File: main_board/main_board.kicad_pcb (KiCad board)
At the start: 4 copper layers, 50 x 50 mm, 80 parts, among them J1 USB Port, J2 I2C, J3 LED, J4 Left_Mic, J5 Left_Speaker, J6 Right_Mic, J7 Right_Speaker, J8 I2C, Q1 MMBT3904, Q2 MMBT3904, SW1 SW_Push, SW2 SW_Push, SW3 SW_Push, U1 AMS1117-3.3, U2 CH340K, U4 Headphone Jack, U5 WM8988LGECN/V, U6 WM8988LGECN/V, U7 AMS1117-3.3, U8 ESP32-WROOM-32E

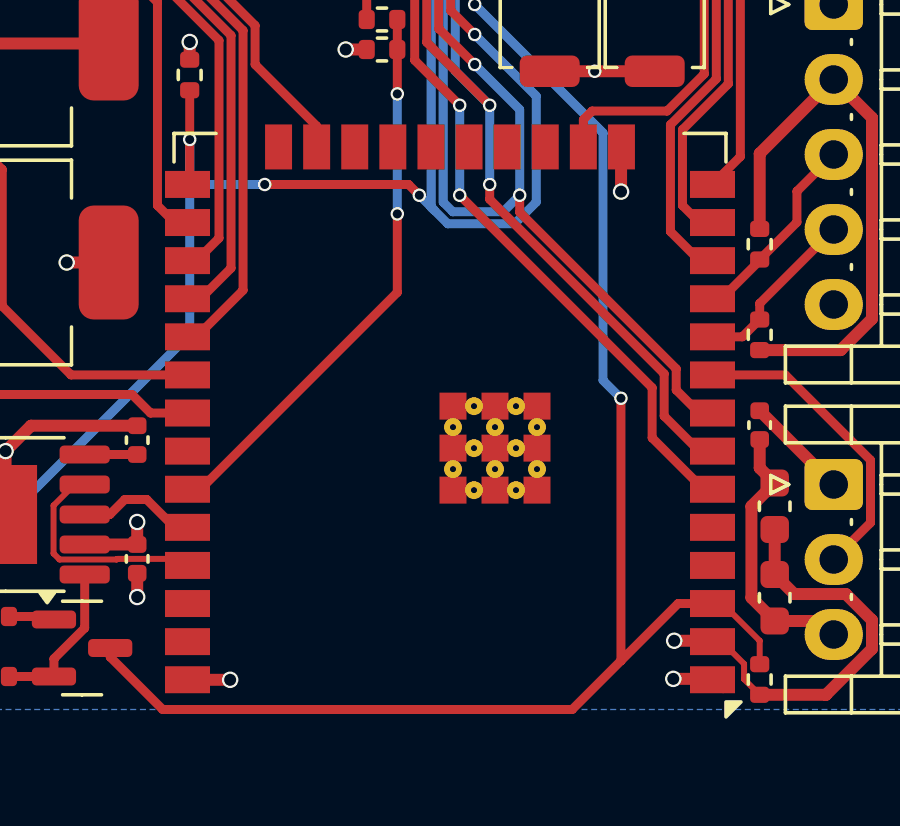
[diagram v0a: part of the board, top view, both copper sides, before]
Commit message: reroute SPI (non output pin issue)
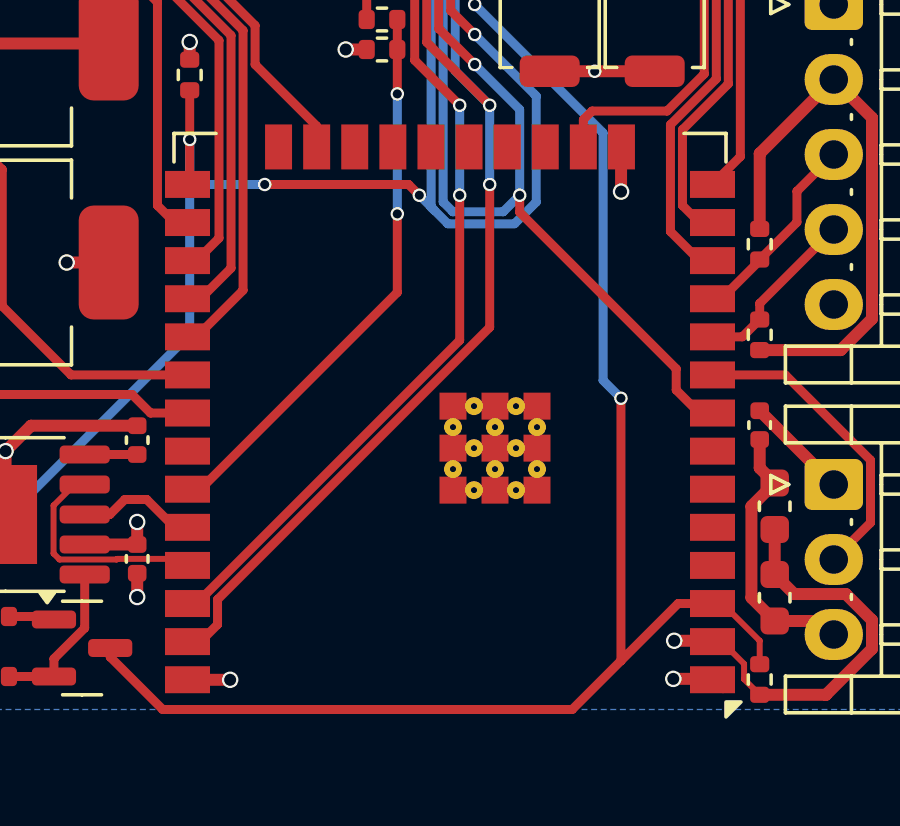
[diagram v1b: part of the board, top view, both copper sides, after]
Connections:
- U8 pad 36: unconnected-(U8-IO22-Pad36) -> /Int->Ext_Select
- U8 pad 37: unconnected-(U8-IO23-Pad37) -> /MOSI
- U8 pad 6: /Int->Ext_Select -> unconnected-(U8-IO34-Pad6)
- U8 pad 7: /MOSI -> unconnected-(U8-IO35-Pad7)
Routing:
- net /MOSI: track 55.5 -> 62.9 mm
- net /Int->Ext_Select: track 29.6 -> 33.7 mm
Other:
- board text added: "CosplayCore V1.1"
- board text removed: "CosplayCore V1.0"
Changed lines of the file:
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@@
 	(net 66 "unconnected-(U6-RINPUT2-Pad21)")
 	(net 67 "/Ext->Int_Select")
-	(net 68 "unconnected-(U8-IO22-Pad36)")
+	(net 68 "unconnected-(U8-IO34-Pad6)")
 	(net 69 "unconnected-(U8-NC-Pad22)")
 	(net 70 "unconnected-(U8-SENSOR_VP-Pad4)")
@@
 	(net 74 "unconnected-(U8-NC-Pad20)")
 	(net 75 "unconnected-(U8-SENSOR_VN-Pad5)")
-	(net 76 "unconnected-(U8-IO23-Pad37)")
+	(net 76 "unconnected-(U8-IO35-Pad7)")
 	(net 77 "unconnected-(U8-NC-Pad19)")
 	(net 78 "unconnected-(U8-NC-Pad32)")
@@
 		(sheetname "/")
 		(sheetfile "main_board.kicad_sch")
-		(attr through_hole exclude_from_pos_files exclude_from_bom)
+		(attr through_hole exclude_from_pos_files)
 		(fp_line
 			(start -0.3 2.1)
@@
 		(sheetname "/")
 		(sheetfile "main_board.kicad_sch")
-		(attr through_hole exclude_from_pos_files exclude_from_bom)
+		(attr through_hole exclude_from_pos_files)
 		(fp_line
 			(start 12.61 -6.81)
@@
 		(sheetname "/")
 		(sheetfile "main_board.kicad_sch")
-		(attr through_hole exclude_from_pos_files exclude_from_bom)
+		(attr through_hole exclude_from_pos_files)
 		(fp_line
 			(start -0.3 2.1)
@@
 		(sheetname "/")
 		(sheetfile "main_board.kicad_sch")
-		(attr through_hole exclude_from_pos_files exclude_from_bom)
+		(attr through_hole exclude_from_pos_files)
 		(fp_line
 			(start 5.11 -6.81)
@@
 		(sheetname "/")
 		(sheetfile "main_board.kicad_sch")
-		(attr through_hole exclude_from_pos_files exclude_from_bom)
+		(attr through_hole exclude_from_pos_files)
 		(fp_line
 			(start 2 5.5)
@@
 			(size 1.5 0.9)
 			(layers "F.Cu" "F.Mask" "F.Paste")
-			(net 28 "/Int->Ext_Select")
+			(net 68 "unconnected-(U8-IO34-Pad6)")
 			(pinfunction "IO34")
-			(pintype "input")
+			(pintype "input+no_connect")
 		)
 		(pad "7" smd rect
@@
 			(size 1.5 0.9)
 			(layers "F.Cu" "F.Mask" "F.Paste")
-			(net 14 "/MOSI")
+			(net 76 "unconnected-(U8-IO35-Pad7)")
 			(pinfunction "IO35")
-			(pintype "input")
+			(pintype "input+no_connect")
 		)
 		(pad "8" smd rect
@@
 			(size 1.5 0.9)
 			(layers "F.Cu" "F.Mask" "F.Paste")
-			(net 68 "unconnected-(U8-IO22-Pad36)")
+			(net 28 "/Int->Ext_Select")
 			(pinfunction "IO22")
-			(pintype "bidirectional+no_connect")
+			(pintype "bidirectional")
 		)
 		(pad "37" smd rect
@@
 			(size 1.5 0.9)
 			(layers "F.Cu" "F.Mask" "F.Paste")
-			(net 76 "unconnected-(U8-IO23-Pad37)")
+			(net 14 "/MOSI")
 			(pinfunction "IO23")
-			(pintype "bidirectional+no_connect")
+			(pintype "bidirectional")
 		)
 		(pad "38" smd rect
@@
 		(sheetname "/")
 		(sheetfile "main_board.kicad_sch")
-		(attr through_hole exclude_from_pos_files exclude_from_bom)
+		(attr through_hole exclude_from_pos_files)
 		(fp_line
 			(start -0.3 2.1)
@@
 		(sheetname "/")
 		(sheetfile "main_board.kicad_sch")
-		(attr through_hole exclude_from_pos_files exclude_from_bom)
+		(attr through_hole exclude_from_pos_files)
 		(fp_line
 			(start 5.11 -6.81)
@@
 		(sheetname "/")
 		(sheetfile "main_board.kicad_sch")
-		(attr through_hole exclude_from_pos_files exclude_from_bom)
+		(attr through_hole exclude_from_pos_files)
 		(fp_line
 			(start -0.3 2.1)
@@
 		)
 	)
-	(gr_text "CosplayCore V1.0"
+	(gr_text "CosplayCore V1.1"
 		(at 139.5 122.325 180)
 		(layer "B.SilkS")
@@
 	)
 	(segment
-		(start 160.31545 108.308053)
-		(end 160.31545 109.718328)
+		(start 134.309299 89.190701)
+		(end 134 89.5)
 		(width 0.3)
 		(layer "F.Cu")
@@
 	)
 	(segment
-		(start 154.5 102)
-		(end 154.5 102.492603)
+		(start 154.5 99.358403)
+		(end 152.401 97.259403)
 		(width 0.3)
 		(layer "F.Cu")
@@
 	)
 	(segment
-		(start 160.31545 109.718328)
-		(end 161.487122 110.89)
+		(start 145.42765 116.668678)
+		(end 145.42765 115.833778)
 		(width 0.3)
 		(layer "F.Cu")
@@
 	)
 	(segment
-		(start 134.309299 89.190701)
-		(end 134 89.5)
+		(start 152.401 97.259403)
+		(end 152.401 92.0958)
 		(width 0.3)
 		(layer "F.Cu")
@@
 	)
 	(segment
-		(start 154.5 102.492603)
-		(end 160.31545 108.308053)
+		(start 144.42665 117.237678)
+		(end 144.85865 117.237678)
 		(width 0.3)
 		(layer "F.Cu")
@@
 	)
 	(segment
-		(start 154.5 99.358403)
-		(end 152.401 97.259403)
+		(start 145.42765 115.833778)
+		(end 154.5 106.761428)
 		(width 0.3)
 		(layer "F.Cu")
@@
 	)
 	(segment
-		(start 152.401 97.259403)
-		(end 152.401 92.0958)
+		(start 152.401 92.0958)
+		(end 155.306099 89.190701)
 		(width 0.3)
 		(layer "F.Cu")
@@
 	)
 	(segment
-		(start 152.401 92.0958)
-		(end 155.306099 89.190701)
+		(start 134.809299 89.190701)
+		(end 134.309299 89.190701)
 		(width 0.3)
 		(layer "F.Cu")
@@
 	)
 	(segment
-		(start 134.809299 89.190701)
-		(end 134.309299 89.190701)
+		(start 144.85865 117.237678)
+		(end 145.42765 116.668678)
 		(width 0.3)
 		(layer "F.Cu")
@@
 	)
 	(segment
-		(start 155.306099 89.190701)
-		(end 155.809299 89.190701)
+		(start 154.5 106.761428)
+		(end 154.5 102)
 		(width 0.3)
 		(layer "F.Cu")
@@
 	)
 	(segment
-		(start 161.487122 110.89)
-		(end 161.919122 110.89)
+		(start 155.306099 89.190701)
+		(end 155.809299 89.190701)
 		(width 0.3)
 		(layer "F.Cu")
@@
 	)
 	(segment
-		(start 153.5 102.358403)
-		(end 159.91445 108.772853)
+		(start 153.5 107.194328)
+		(end 153.5 102.358403)
 		(width 0.3)
 		(layer "F.Cu")
@@
 	)
 	(segment
-		(start 152 97.858403)
-		(end 152 91.9297)
+		(start 144.72665 115.967678)
+		(end 153.5 107.194328)
 		(width 0.3)
 		(layer "F.Cu")
@@
 	)
 	(segment
-		(start 159.91445 110.445478)
-		(end 161.62665 112.157678)
+		(start 152 97.858403)
+		(end 152 91.9297)
 		(width 0.3)
 		(layer "F.Cu")
@@
 	)
 	(segment
-		(start 155.189001 88.740699)
-		(end 155.809299 88.740699)
+		(start 144.42665 115.967678)
+		(end 144.72665 115.967678)
 		(width 0.3)
 		(layer "F.Cu")
@@
 	)
 	(segment
-		(start 153.5 99.358403)
-		(end 152 97.858403)
-		(width 0.3)
-		(layer "F.Cu")
-		(net 28)
-	)
-	(segment
-		(start 159.91445 108.772853)
-		(end 159.91445 110.445478)
+		(start 155.189001 88.740699)
+		(end 155.809299 88.740699)
 		(width 0.3)
 		(layer "F.Cu")
@@
 	)
 	(segment
-		(start 161.62665 112.157678)
-		(end 161.92665 112.157678)
+		(start 153.5 99.358403)
+		(end 152 97.858403)
 		(width 0.3)
 		(layer "F.Cu")
